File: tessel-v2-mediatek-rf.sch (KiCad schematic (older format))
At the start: 40 parts, among them J501 CONN_01X01, J502 CONN_01X01, J503 CONN_01X03, U201 MT7620N

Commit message: annotated
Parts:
- gave numbers to parts that had none: 2
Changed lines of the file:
@@
 $EndComp
 $Comp
-L GND #PWR029
+L GND #PWR41
 U 1 1 5492119C
 P 10600 4350
-F 0 "#PWR029" H 10600 4350 30  0001 C CNN
+F 0 "#PWR41" H 10600 4350 30  0001 C CNN
 F 1 "GND" H 10600 4280 30  0001 C CNN
 F 2 "" H 10600 4350 60  0000 C CNN
@@
 $EndComp
 $Comp
-L GND #PWR030
+L GND #PWR43
 U 1 1 549211F2
 P 11800 4350
-F 0 "#PWR030" H 11800 4350 30  0001 C CNN
+F 0 "#PWR43" H 11800 4350 30  0001 C CNN
 F 1 "GND" H 11800 4280 30  0001 C CNN
 F 2 "" H 11800 4350 60  0000 C CNN
@@
 $EndComp
 $Comp
-L GND #PWR031
+L GND #PWR45
 U 1 1 54921339
 P 13100 3150
-F 0 "#PWR031" H 13100 3150 30  0001 C CNN
+F 0 "#PWR45" H 13100 3150 30  0001 C CNN
 F 1 "GND" H 13100 3080 30  0001 C CNN
 F 2 "" H 13100 3150 60  0000 C CNN
@@
 $EndComp
 $Comp
-L GND #PWR033
+L GND #PWR34
 U 1 1 54921B0A
 P 5900 4800
-F 0 "#PWR033" H 5900 4800 30  0001 C CNN
+F 0 "#PWR34" H 5900 4800 30  0001 C CNN
 F 1 "GND" H 5900 4730 30  0001 C CNN
 F 2 "" H 5900 4800 60  0000 C CNN
@@
 $EndComp
 $Comp
-L GND #PWR034
+L GND #PWR33
 U 1 1 54921B48
 P 5900 3000
-F 0 "#PWR034" H 5900 3000 30  0001 C CNN
+F 0 "#PWR33" H 5900 3000 30  0001 C CNN
 F 1 "GND" H 5900 2930 30  0001 C CNN
 F 2 "" H 5900 3000 60  0000 C CNN
@@
 $EndComp
 $Comp
-L GND #PWR036
+L GND #PWR42
 U 1 1 5492F3B9
 P 10600 7250
-F 0 "#PWR036" H 10600 7250 30  0001 C CNN
+F 0 "#PWR42" H 10600 7250 30  0001 C CNN
 F 1 "GND" H 10600 7180 30  0001 C CNN
 F 2 "" H 10600 7250 60  0000 C CNN
@@
 $EndComp
 $Comp
-L GND #PWR037
+L GND #PWR44
 U 1 1 5492F3BF
 P 11800 7250
-F 0 "#PWR037" H 11800 7250 30  0001 C CNN
+F 0 "#PWR44" H 11800 7250 30  0001 C CNN
 F 1 "GND" H 11800 7180 30  0001 C CNN
 F 2 "" H 11800 7250 60  0000 C CNN
@@
 $EndComp
 $Comp
-L GND #PWR038
+L GND #PWR46
 U 1 1 5492F3C5
 P 13100 6050
-F 0 "#PWR038" H 13100 6050 30  0001 C CNN
+F 0 "#PWR46" H 13100 6050 30  0001 C CNN
 F 1 "GND" H 13100 5980 30  0001 C CNN
 F 2 "" H 13100 6050 60  0000 C CNN
@@
 $EndComp
 $Comp
-L GND #PWR040
+L GND #PWR36
 U 1 1 5492F3D6
 P 5900 7700
-F 0 "#PWR040" H 5900 7700 30  0001 C CNN
+F 0 "#PWR36" H 5900 7700 30  0001 C CNN
 F 1 "GND" H 5900 7630 30  0001 C CNN
 F 2 "" H 5900 7700 60  0000 C CNN
@@
 $EndComp
 $Comp
-L GND #PWR041
+L GND #PWR35
 U 1 1 5492F3DC
 P 5900 5900
-F 0 "#PWR041" H 5900 5900 30  0001 C CNN
+F 0 "#PWR35" H 5900 5900 30  0001 C CNN
 F 1 "GND" H 5900 5830 30  0001 C CNN
 F 2 "" H 5900 5900 60  0000 C CNN
@@
 $EndComp
 $Comp
-L +3.3V #PWR043
+L +3.3V #PWR30
 U 1 1 54916FFB
 P 4200 5450
-F 0 "#PWR043" H 4200 5410 30  0001 C CNN
+F 0 "#PWR30" H 4200 5410 30  0001 C CNN
 F 1 "+3.3V" H 4200 5560 30  0000 C CNN
 F 2 "" H 4200 5450 60  0000 C CNN
@@
 $EndComp
 $Comp
-L GND #PWR044
+L GND #PWR29
 U 1 1 54917BEF
 P 2050 5950
-F 0 "#PWR044" H 2050 5950 30  0001 C CNN
+F 0 "#PWR29" H 2050 5950 30  0001 C CNN
 F 1 "GND" H 2050 5880 30  0001 C CNN
 F 2 "" H 2050 5950 60  0000 C CNN
@@
 NC_78
 $Comp
-L GND #PWR045
+L GND #PWR31
 U 1 1 54918F7B
 P 4900 5750
-F 0 "#PWR045" H 4900 5750 30  0001 C CNN
+F 0 "#PWR31" H 4900 5750 30  0001 C CNN
 F 1 "GND" H 4900 5680 30  0001 C CNN
 F 2 "" H 4900 5750 60  0000 C CNN
@@
 $EndComp
 $Comp
-L +3.3V #PWR046
+L +3.3V #PWR32
 U 1 1 54919282
 P 5350 5600
-F 0 "#PWR046" H 5350 5560 30  0001 C CNN
+F 0 "#PWR32" H 5350 5560 30  0001 C CNN
 F 1 "+3.3V" H 5350 5710 30  0000 C CNN
 F 2 "" H 5350 5600 60  0000 C CNN
@@
 ANT_TRNB: XTAL_FREQ_SEL\n0 = 20MHz\n1 = 40MHz
 $Comp
-L 2450BL15B100 T?
+L 2450BL15B100 T1
 U 1 1 54BF6A48
 P 9600 3950
-F 0 "T?" H 9250 4300 60  0000 C CNN
+F 0 "T1" H 9250 4300 60  0000 C CNN
 F 1 "2450BL15B100" H 9600 4000 60  0000 C CNN
 F 2 "" H 9600 3950 60  0000 C CNN
@@
 	8900 4050 9000 4050
 $Comp
-L 2450BL15B100 T?
+L 2450BL15B100 T2
 U 1 1 54BF8042
 P 9600 6850
-F 0 "T?" H 9250 7200 60  0000 C CNN
+F 0 "T2" H 9250 7200 60  0000 C CNN
 F 1 "2450BL15B100" H 9600 6900 60  0000 C CNN
 F 2 "" H 9600 6850 60  0000 C CNN
@@
 	10300 6950 10300 7250
 $Comp
-L GND #PWR?
+L GND #PWR40
 U 1 1 54BF867B
 P 10300 7250
-F 0 "#PWR?" H 10300 7250 30  0001 C CNN
+F 0 "#PWR40" H 10300 7250 30  0001 C CNN
 F 1 "GND" H 10300 7180 30  0001 C CNN
 F 2 "" H 10300 7250 60  0000 C CNN
@@
 	9500 7550 9500 7450
 $Comp
-L GND #PWR?
+L GND #PWR38
 U 1 1 54BF87B3
 P 9500 7550
-F 0 "#PWR?" H 9500 7550 30  0001 C CNN
+F 0 "#PWR38" H 9500 7550 30  0001 C CNN
 F 1 "GND" H 9500 7480 30  0001 C CNN
 F 2 "" H 9500 7550 60  0000 C CNN
@@
 	9500 4650 9500 4550
 $Comp
-L GND #PWR?
+L GND #PWR37
 U 1 1 54BF88AF
 P 9500 4650
-F 0 "#PWR?" H 9500 4650 30  0001 C CNN
+F 0 "#PWR37" H 9500 4650 30  0001 C CNN
 F 1 "GND" H 9500 4580 30  0001 C CNN
 F 2 "" H 9500 4650 60  0000 C CNN
@@
 	10300 4050 10300 4350
 $Comp
-L GND #PWR?
+L GND #PWR39
 U 1 1 54BF89CF
 P 10300 4350
-F 0 "#PWR?" H 10300 4350 30  0001 C CNN
+F 0 "#PWR39" H 10300 4350 30  0001 C CNN
 F 1 "GND" H 10300 4280 30  0001 C CNN
 F 2 "" H 10300 4350 60  0000 C CNN

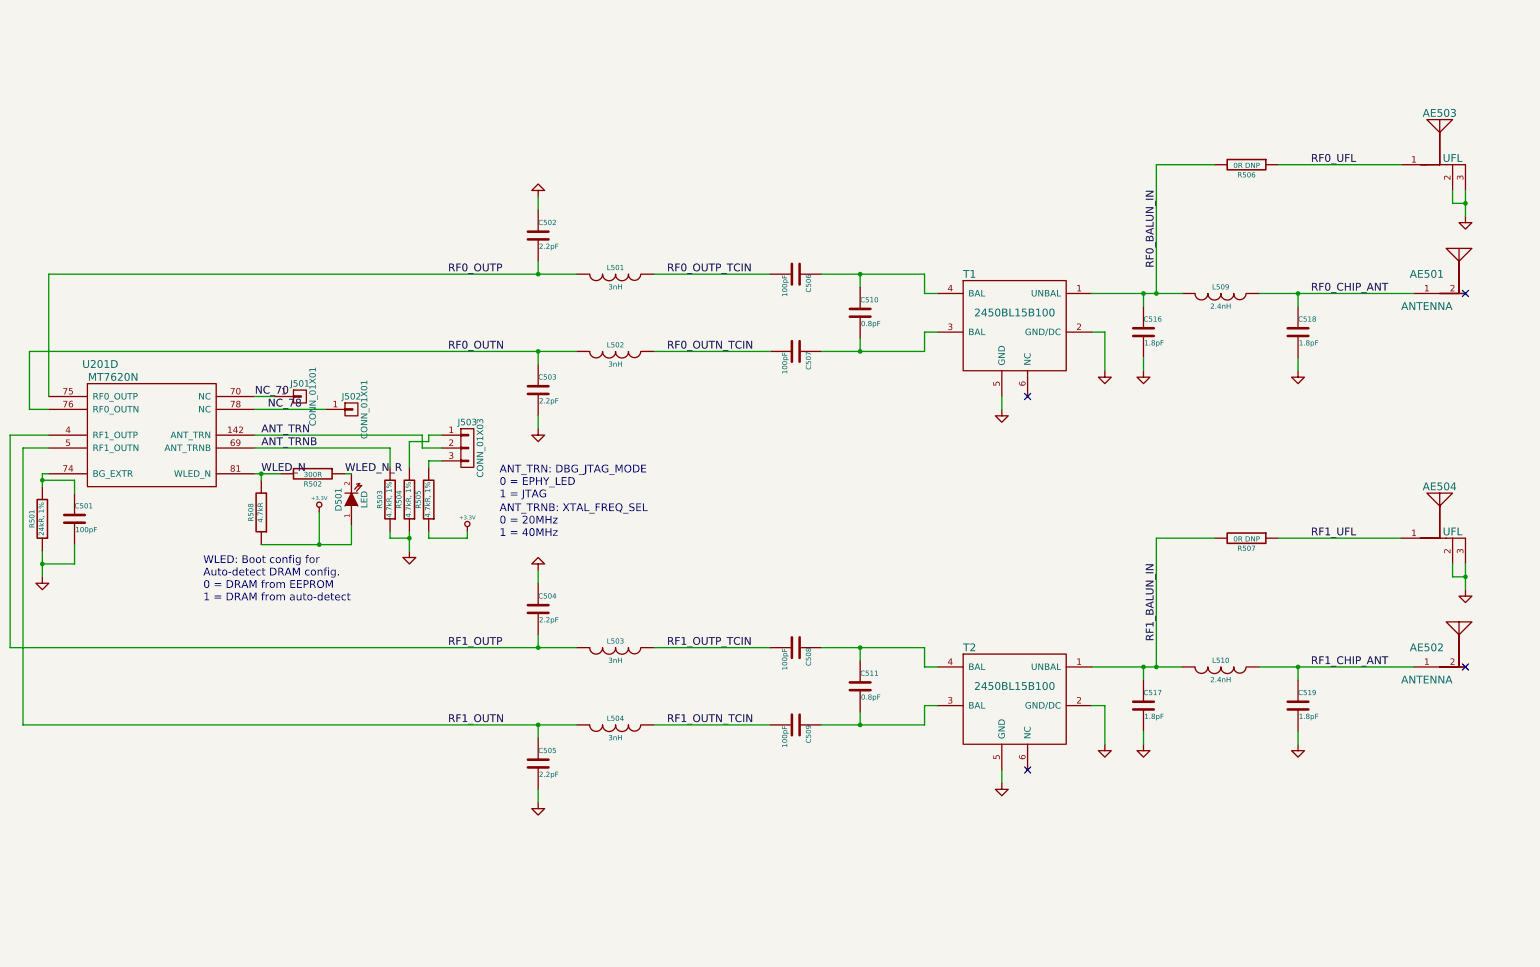
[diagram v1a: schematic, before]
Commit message: added pcb antennas, more annotation
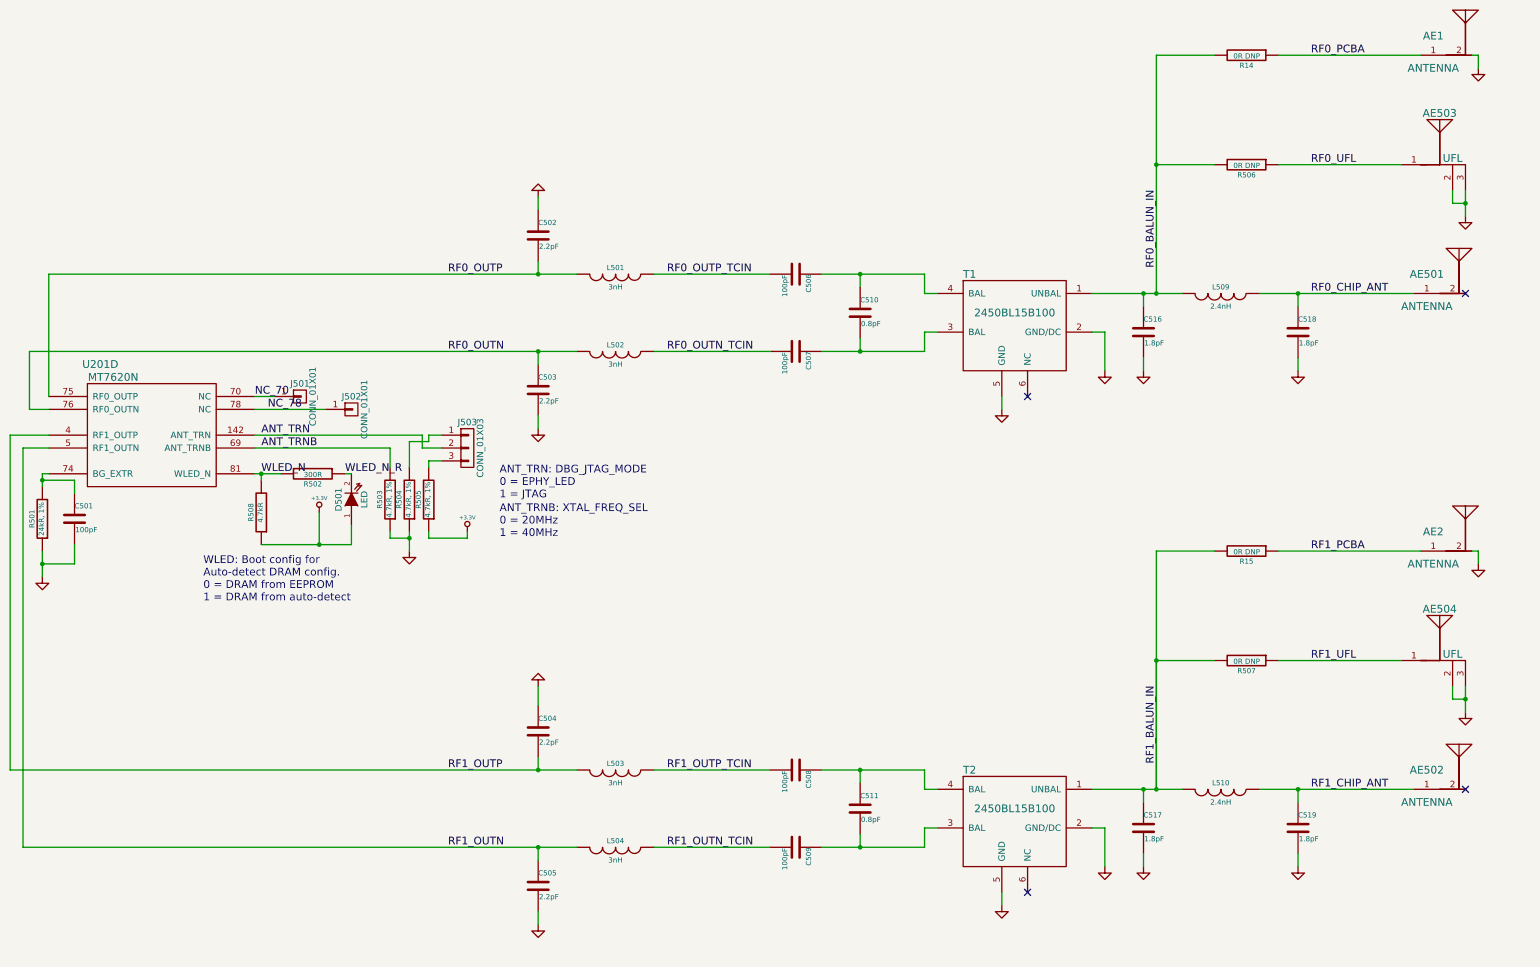
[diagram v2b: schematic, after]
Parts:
- added AE1, AE2: ANTENNA, tm-kicad-lib:ANTENNA-SMT-2.45GHz, symbol ANTENNA
- added R14, R15: 0R DNP, tm-kicad-lib:SMD-0402, symbol R
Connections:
- net GND: now also AE1.2, AE2.2
- net RF0_BALUN_IN: now also R14.2
- net RF1_BALUN_IN: now also R15.2
- new net RF0_PCBA: AE1.1, R14.1
- new net RF1_PCBA: AE2.1, R15.1
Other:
- moved on the sheet: AE502, AE504, C504, C505, C508, C509, C511, C517, C519, L503, L504, L510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

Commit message: apologies jia... needed to re-number things
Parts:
- renumbered AE1 to AE503, AE2 to AE504, AE503 to AE505, AE504 to AE506, C516 to C512, C517 to C513, C518 to C514, C519 to C515, L509 to L505, L510 to L506, R508 to R502, R502 to R503, R503 to R504, R504 to R505, R505 to R506, R14 to R507, R506 to R508, R15 to R509, R507 to R510, T1 to T501, T2 to T502

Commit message: swd/jtag pinswaps and LEDs
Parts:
- D501: value LED -> AMBER
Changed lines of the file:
@@
 P 4450 5350
 F 0 "D501" H 4450 5450 50  0000 C CNN
-F 1 "LED" H 4450 5250 50  0000 C CNN
+F 1 "AMBER" H 4450 5250 50  0000 C CNN
 F 2 "LEDs:LED-0603" H 4450 5350 60  0001 C CNN
 F 3 "" H 4450 5350 60  0000 C CNN

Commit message: re-re-re-etc. annotate
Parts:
- removed J503: CONN_01X03, Pin_Headers:Pin_Header_Straight_1x03, symbol CONN_01X03
- R505: value 4.7kR, 1% -> 4.7kR, DNP
- R506: value 4.7kR, 1% -> 4.7kR
- renumbered AE505 to AE503, AE506 to AE504, AE503 to AE505, AE504 to AE506, R508 to R507, R510 to R508, R507 to R509, R509 to R510
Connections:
- net ANT_TRN: now also R505.2, R506.2
- net RF0_CHIP_ANT: now also R509.2
- net RF1_CHIP_ANT: now also R510.2
- net RF0_BALUN_IN_P: now reaches C506.1, C510.1, T501.4 (BAL)
- net RF0_BALUN_IN_N: now reaches C507.1, C510.2, T501.3 (BAL)
- net RF1_BALUN_IN_P: now reaches C508.1, C511.1, T502.4 (BAL)
- net RF1_BALUN_IN_N: now reaches C509.1, C511.2, T502.3 (BAL)
- net RF0_BALUN_IN renamed RF0_BALUN_OUT
- net RF0_BALUN_OUT: no longer R509.2
- net RF1_BALUN_IN renamed RF1_BALUN_OUT
- net RF1_BALUN_OUT: no longer R510.2
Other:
- moved on the sheet: AE505, AE506, C514, C515, R509, R510

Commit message: swapped to "X DNP" from "X, DNP"; reassign and whatnot
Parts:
- AE505, AE506: footprint tm-kicad-lib:ANTENNA-SMT-2.45GHz -> !Parts:2.4GHz-INVERTED-F-ANTENNA
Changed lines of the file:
@@
 $EndComp
 $Comp
-L GND #PWR513
+L GND #PWR031
 U 1 1 5492119C
 P 10600 4350
-F 0 "#PWR513" H 10600 4350 30  0001 C CNN
+F 0 "#PWR031" H 10600 4350 30  0001 C CNN
 F 1 "GND" H 10600 4280 30  0001 C CNN
 F 2 "" H 10600 4350 60  0000 C CNN
@@
 $EndComp
 $Comp
-L GND #PWR515
+L GND #PWR032
 U 1 1 549211F2
 P 11800 4900
-F 0 "#PWR515" H 11800 4900 30  0001 C CNN
+F 0 "#PWR032" H 11800 4900 30  0001 C CNN
 F 1 "GND" H 11800 4830 30  0001 C CNN
 F 2 "" H 11800 4900 60  0000 C CNN
@@
 $EndComp
 $Comp
-L GND #PWR517
+L GND #PWR033
 U 1 1 54921339
 P 13100 3150
-F 0 "#PWR517" H 13100 3150 30  0001 C CNN
+F 0 "#PWR033" H 13100 3150 30  0001 C CNN
 F 1 "GND" H 13100 3080 30  0001 C CNN
 F 2 "" H 13100 3150 60  0000 C CNN
@@
 $EndComp
 $Comp
-L GND #PWR506
+L GND #PWR034
 U 1 1 54921B0A
 P 5900 4800
-F 0 "#PWR506" H 5900 4800 30  0001 C CNN
+F 0 "#PWR034" H 5900 4800 30  0001 C CNN
 F 1 "GND" H 5900 4730 30  0001 C CNN
 F 2 "" H 5900 4800 60  0000 C CNN
@@
 $EndComp
 $Comp
-L GND #PWR505
+L GND #PWR035
 U 1 1 54921B48
 P 5900 3000
-F 0 "#PWR505" H 5900 3000 30  0001 C CNN
+F 0 "#PWR035" H 5900 3000 30  0001 C CNN
 F 1 "GND" H 5900 2930 30  0001 C CNN
 F 2 "" H 5900 3000 60  0000 C CNN
@@
 $EndComp
 $Comp
-L GND #PWR514
+L GND #PWR036
 U 1 1 5492F3B9
 P 10600 8200
-F 0 "#PWR514" H 10600 8200 30  0001 C CNN
+F 0 "#PWR036" H 10600 8200 30  0001 C CNN
 F 1 "GND" H 10600 8130 30  0001 C CNN
 F 2 "" H 10600 8200 60  0000 C CNN
@@
 $EndComp
 $Comp
-L GND #PWR516
+L GND #PWR037
 U 1 1 5492F3BF
 P 11800 8800
-F 0 "#PWR516" H 11800 8800 30  0001 C CNN
+F 0 "#PWR037" H 11800 8800 30  0001 C CNN
 F 1 "GND" H 11800 8730 30  0001 C CNN
 F 2 "" H 11800 8800 60  0000 C CNN
@@
 $EndComp
 $Comp
-L GND #PWR518
+L GND #PWR038
 U 1 1 5492F3C5
 P 13100 7000
-F 0 "#PWR518" H 13100 7000 30  0001 C CNN
+F 0 "#PWR038" H 13100 7000 30  0001 C CNN
 F 1 "GND" H 13100 6930 30  0001 C CNN
 F 2 "" H 13100 7000 60  0000 C CNN
@@
 $EndComp
 $Comp
-L GND #PWR508
+L GND #PWR039
 U 1 1 5492F3D6
 P 5900 8650
-F 0 "#PWR508" H 5900 8650 30  0001 C CNN
+F 0 "#PWR039" H 5900 8650 30  0001 C CNN
 F 1 "GND" H 5900 8580 30  0001 C CNN
 F 2 "" H 5900 8650 60  0000 C CNN
@@
 $EndComp
 $Comp
-L GND #PWR507
+L GND #PWR040
 U 1 1 5492F3DC
 P 5900 6800
-F 0 "#PWR507" H 5900 6800 30  0001 C CNN
+F 0 "#PWR040" H 5900 6800 30  0001 C CNN
 F 1 "GND" H 5900 6730 30  0001 C CNN
 F 2 "" H 5900 6800 60  0000 C CNN
@@
 $EndComp
 $Comp
-L +3.3V #PWR502
+L +3.3V #PWR041
 U 1 1 54916FFB
 P 4200 5450
-F 0 "#PWR502" H 4200 5410 30  0001 C CNN
+F 0 "#PWR041" H 4200 5410 30  0001 C CNN
 F 1 "+3.3V" H 4200 5560 30  0000 C CNN
 F 2 "" H 4200 5450 60  0000 C CNN
@@
 $EndComp
 $Comp
-L GND #PWR501
+L GND #PWR042
 U 1 1 54917BEF
 P 2050 5950
-F 0 "#PWR501" H 2050 5950 30  0001 C CNN
+F 0 "#PWR042" H 2050 5950 30  0001 C CNN
 F 1 "GND" H 2050 5880 30  0001 C CNN
 F 2 "" H 2050 5950 60  0000 C CNN
@@
 $EndComp
 Wire Wire Line
-	11800 4400 11800 4200
-Wire Wire Line
-	11800 4200 11800 3750
+	11800 3750 11800 4400
 Connection ~ 11800 3750
 Wire Wire Line
@@
 	7700 4200 6800 4200
 Wire Wire Line
-	1950 4200 5900 4200
-Wire Wire Line
-	5900 4200 6200 4200
+	1950 4200 6200 4200
 Wire Wire Line
 	5900 4300 5900 4200
 Connection ~ 5900 4200
 Wire Wire Line
-	2100 3600 5900 3600
-Wire Wire Line
-	5900 3600 6200 3600
+	2100 3600 6200 3600
 Wire Wire Line
 	6800 3600 7700 3600
@@
 	10600 4250 10600 4350
 Wire Wire Line
-	13100 2950 13100 3050
-Wire Wire Line
-	13100 3050 13100 3150
+	13100 2950 13100 3150
 Wire Wire Line
 	13100 3050 13000 3050
@@
 Connection ~ 10700 3750
 Wire Wire Line
-	11500 3750 11800 3750
-Wire Wire Line
-	11800 3750 12700 3750
+	11500 3750 12700 3750
 Wire Wire Line
 	11650 2750 12600 2750
 Wire Wire Line
-	11800 8300 11800 8100
-Wire Wire Line
-	11800 8100 11800 7600
+	11800 7600 11800 8300
 Connection ~ 11800 7600
 Wire Wire Line
@@
 	7700 8050 6800 8050
 Wire Wire Line
-	1900 8050 5900 8050
-Wire Wire Line
-	5900 8050 6200 8050
+	1900 8050 6200 8050
 Wire Wire Line
 	5900 8150 5900 8050
 Connection ~ 5900 8050
 Wire Wire Line
-	1800 7450 5900 7450
-Wire Wire Line
-	5900 7450 6200 7450
+	1800 7450 6200 7450
 Wire Wire Line
 	6800 7450 7700 7450
@@
 	10600 8100 10600 8200
 Wire Wire Line
-	13100 6800 13100 6900
-Wire Wire Line
-	13100 6900 13100 7000
+	13100 6800 13100 7000
 Wire Wire Line
 	13100 6900 13000 6900
@@
 Connection ~ 10700 7600
 Wire Wire Line
-	11500 7600 11800 7600
-Wire Wire Line
-	11800 7600 12700 7600
+	11500 7600 12700 7600
 Wire Wire Line
 	11650 6600 12600 6600
@@
 	4400 5150 4450 5150
 Wire Wire Line
-	3700 5150 3750 5150
-Wire Wire Line
-	3750 5150 3900 5150
+	3700 5150 3900 5150
 Wire Wire Line
 	4450 5700 4450 5550
 Wire Wire Line
-	2050 5150 2050 5200
-Wire Wire Line
-	2050 5200 2050 5250
+	2050 5150 2050 5250
 Wire Wire Line
 	2050 5150 2100 5150
 Wire Wire Line
-	2050 5750 2050 5850
-Wire Wire Line
-	2050 5850 2050 5950
+	2050 5750 2050 5950
 Wire Wire Line
 	2300 5300 2300 5200
@@
 NC_78
 $Comp
-L GND #PWR503
+L GND #PWR043
 U 1 1 54918F7B
 P 4900 5750
-F 0 "#PWR503" H 4900 5750 30  0001 C CNN
+F 0 "#PWR043" H 4900 5750 30  0001 C CNN
 F 1 "GND" H 4900 5680 30  0001 C CNN
 F 2 "" H 4900 5750 60  0000 C CNN
@@
 	4200 5450 4200 5700
 Wire Wire Line
-	3750 5700 4200 5700
-Wire Wire Line
-	4200 5700 4450 5700
+	3750 5700 4450 5700
 $Comp
 L R R506
@@
 $EndComp
 $Comp
-L +3.3V #PWR504
+L +3.3V #PWR044
 U 1 1 54919282
 P 5200 5550
-F 0 "#PWR504" H 5200 5510 30  0001 C CNN
+F 0 "#PWR044" H 5200 5510 30  0001 C CNN
 F 1 "+3.3V" H 5200 5660 30  0000 C CNN
 F 2 "" H 5200 5550 60  0000 C CNN
@@
 	4750 5650 4750 5600
 Wire Wire Line
-	4900 5600 4900 5650
-Wire Wire Line
-	4900 5650 4900 5750
+	4900 5600 4900 5750
 Connection ~ 4900 5650
 Wire Wire Line
@@
 F 0 "T501" H 9250 4300 60  0000 C CNN
 F 1 "2450BL15B100" H 9600 4000 60  0000 C CNN
-F 2 "" H 9600 3950 60  0000 C CNN
+F 2 "" H 9600 3950 60  0001 C CNN
 F 3 "" H 9600 3950 60  0000 C CNN
 	1    9600 3950
@@
 $EndComp
 Wire Wire Line
-	10200 3750 10600 3750
-Wire Wire Line
-	10600 3750 10700 3750
-Wire Wire Line
-	10700 3750 10900 3750
-Wire Wire Line
-	8100 3600 8400 3600
-Wire Wire Line
-	8400 3600 8900 3600
+	10200 3750 10900 3750
+Wire Wire Line
+	8100 3600 8900 3600
 Wire Wire Line
 	8900 3600 8900 3750
 Wire Wire Line
-	8100 4200 8400 4200
-Wire Wire Line
-	8400 4200 8900 4200
+	8100 4200 8900 4200
 Wire Wire Line
 	8900 4200 8900 4050
@@
 F 0 "T502" H 9250 8150 60  0000 C CNN
 F 1 "2450BL15B100" H 9600 7850 60  0000 C CNN
-F 2 "" H 9600 7800 60  0000 C CNN
+F 2 "" H 9600 7800 60  0001 C CNN
 F 3 "" H 9600 7800 60  0000 C CNN
 	1    9600 7800
@@
 $EndComp
 Wire Wire Line
-	8100 7450 8400 7450
-Wire Wire Line
-	8400 7450 8900 7450
+	8100 7450 8900 7450
 Wire Wire Line
 	8900 7450 8900 7600
 Wire Wire Line
-	8100 8050 8400 8050
-Wire Wire Line
-	8400 8050 8900 8050
+	8100 8050 8900 8050
 Wire Wire Line
 	8900 8050 8900 7900
@@
 	8900 7900 9000 7900
 Wire Wire Line
-	10200 7600 10600 7600
-Wire Wire Line
-	10600 7600 10700 7600
-Wire Wire Line
-	10700 7600 10900 7600
+	10200 7600 10900 7600
 Wire Wire Line
 	10200 7900 10300 7900
@@
 	10300 7900 10300 8200
 $Comp
-L GND #PWR512
+L GND #PWR045
 U 1 1 54BF867B
 P 10300 8200
-F 0 "#PWR512" H 10300 8200 30  0001 C CNN
+F 0 "#PWR045" H 10300 8200 30  0001 C CNN
 F 1 "GND" H 10300 8130 30  0001 C CNN
 F 2 "" H 10300 8200 60  0000 C CNN
@@
 	9500 8500 9500 8400
 $Comp
-L GND #PWR510
+L GND #PWR046
 U 1 1 54BF87B3
 P 9500 8500
-F 0 "#PWR510" H 9500 8500 30  0001 C CNN
+F 0 "#PWR046" H 9500 8500 30  0001 C CNN
 F 1 "GND" H 9500 8430 30  0001 C CNN
 F 2 "" H 9500 8500 60  0000 C CNN
@@
 	9500 4650 9500 4550
 $Comp
-L GND #PWR509
+L GND #PWR047
 U 1 1 54BF88AF
 P 9500 4650
-F 0 "#PWR509" H 9500 4650 30  0001 C CNN
+F 0 "#PWR047" H 9500 4650 30  0001 C CNN
 F 1 "GND" H 9500 4580 30  0001 C CNN
 F 2 "" H 9500 4650 60  0000 C CNN
@@
 	10300 4050 10300 4350
 $Comp
-L GND #PWR511
+L GND #PWR048
 U 1 1 54BF89CF
 P 10300 4350
-F 0 "#PWR511" H 10300 4350 30  0001 C CNN
+F 0 "#PWR048" H 10300 4350 30  0001 C CNN
 F 1 "GND" H 10300 4280 30  0001 C CNN
 F 2 "" H 10300 4350 60  0000 C CNN
@@
 F 0 "AE505" H 13200 4350 60  0000 C CNN
 F 1 "ANTENNA" H 13200 4100 60  0000 C CNN
-F 2 "tm-kicad-lib:ANTENNA-SMT-2.45GHz" H 13300 4200 60  0001 C CNN
+F 2 "!Parts:2.4GHz-INVERTED-F-ANTENNA" H 13300 4200 60  0001 C CNN
 F 3 "" H 13300 4200 60  0000 C CNN
 	1    13200 4200
@@
 $EndComp
 $Comp
-L GND #PWR519
+L GND #PWR049
 U 1 1 54BF1FF8
 P 13550 4300
-F 0 "#PWR519" H 13550 4300 30  0001 C CNN
+F 0 "#PWR049" H 13550 4300 30  0001 C CNN
 F 1 "GND" H 13550 4230 30  0001 C CNN
 F 2 "" H 13550 4300 60  0000 C CNN
@@
 F 0 "AE506" H 13200 8250 60  0000 C CNN
 F 1 "ANTENNA" H 13200 8000 60  0000 C CNN
-F 2 "tm-kicad-lib:ANTENNA-SMT-2.45GHz" H 13300 8100 60  0001 C CNN
+F 2 "!Parts:2.4GHz-INVERTED-F-ANTENNA" H 13300 8100 60  0001 C CNN
 F 3 "" H 13300 8100 60  0000 C CNN
 	1    13200 8100
@@
 $EndComp
 $Comp
-L GND #PWR520
+L GND #PWR050
 U 1 1 54BF258A
 P 13550 8200
-F 0 "#PWR520" H 13550 8200 30  0001 C CNN
+F 0 "#PWR050" H 13550 8200 30  0001 C CNN
 F 1 "GND" H 13550 8130 30  0001 C CNN
 F 2 "" H 13550 8200 60  0000 C CNN
@@
 RF1_PCBA
 Wire Wire Line
-	3700 4850 4900 4850
-Wire Wire Line
-	4900 4850 5050 4850
+	3700 4850 5050 4850
 Wire Wire Line
 	5050 4850 5050 5100
@@
 RF0_BALUN_IN_P
 Wire Wire Line
-	10700 3750 10700 2750
+	10700 2750 10700 3750
 Wire Wire Line
 	10700 6600 10700 7600
